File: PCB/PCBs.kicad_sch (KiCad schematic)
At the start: 55 parts, among them CN1 W2A41C681KAT2A, CN2 W2A41C681KAT2A, CN3 W2A41C681KAT2A, CN4 W2A41C681KAT2A, CN6 W2A41C681KAT2A, U1 ADS1299IPAGR, U10 TPD4E1B06DCKR, U11 TPS61023DRLR, U3 TPD4E1B06DCKR, U4 TPD4E1B06DCKR, U5 TPS73225DBVR, U6 TPD4E1B06DCKR, U7 LM2664M6, U8 TPS73233DBVT, U9 TPS72325DBVT

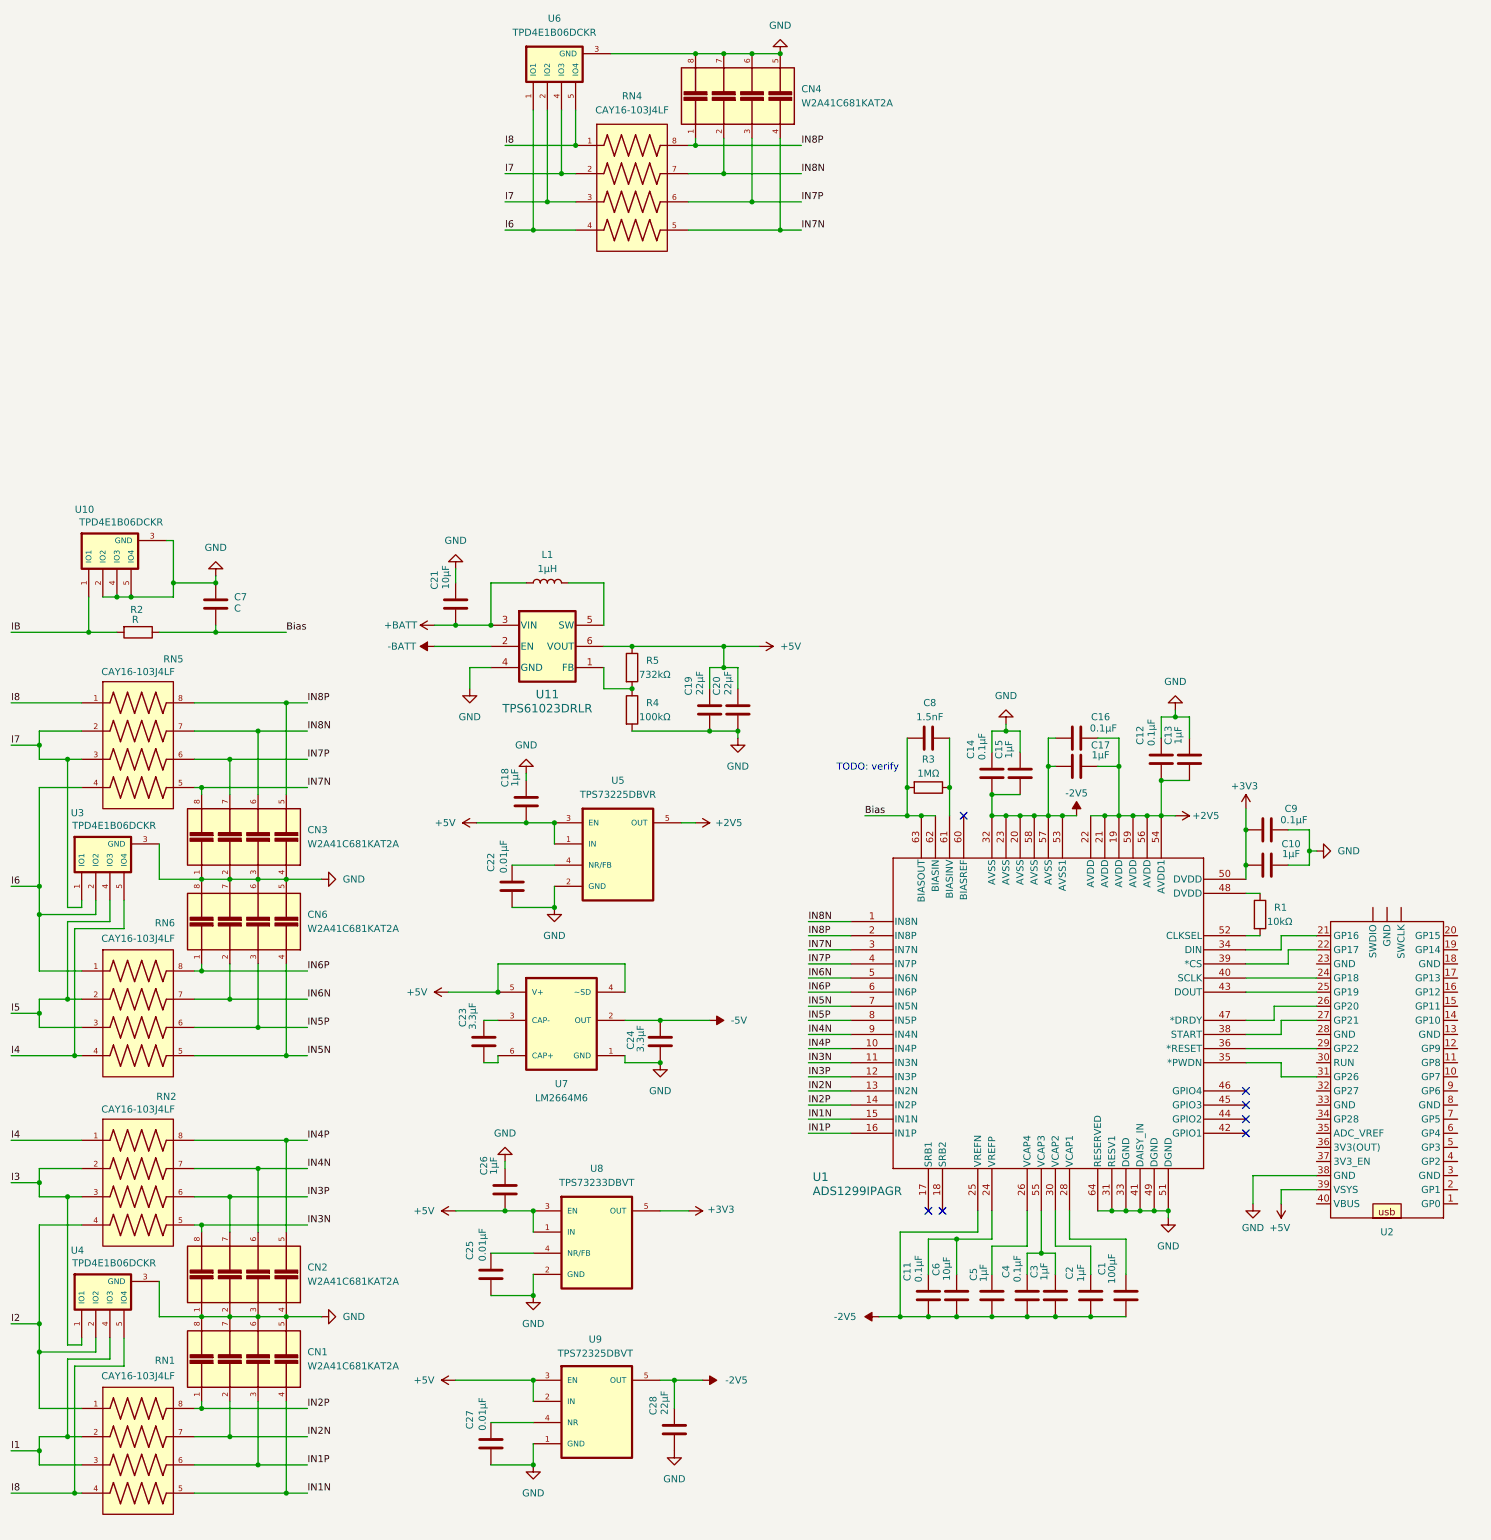
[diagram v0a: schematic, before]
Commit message: v0.1 schematic finishing touches
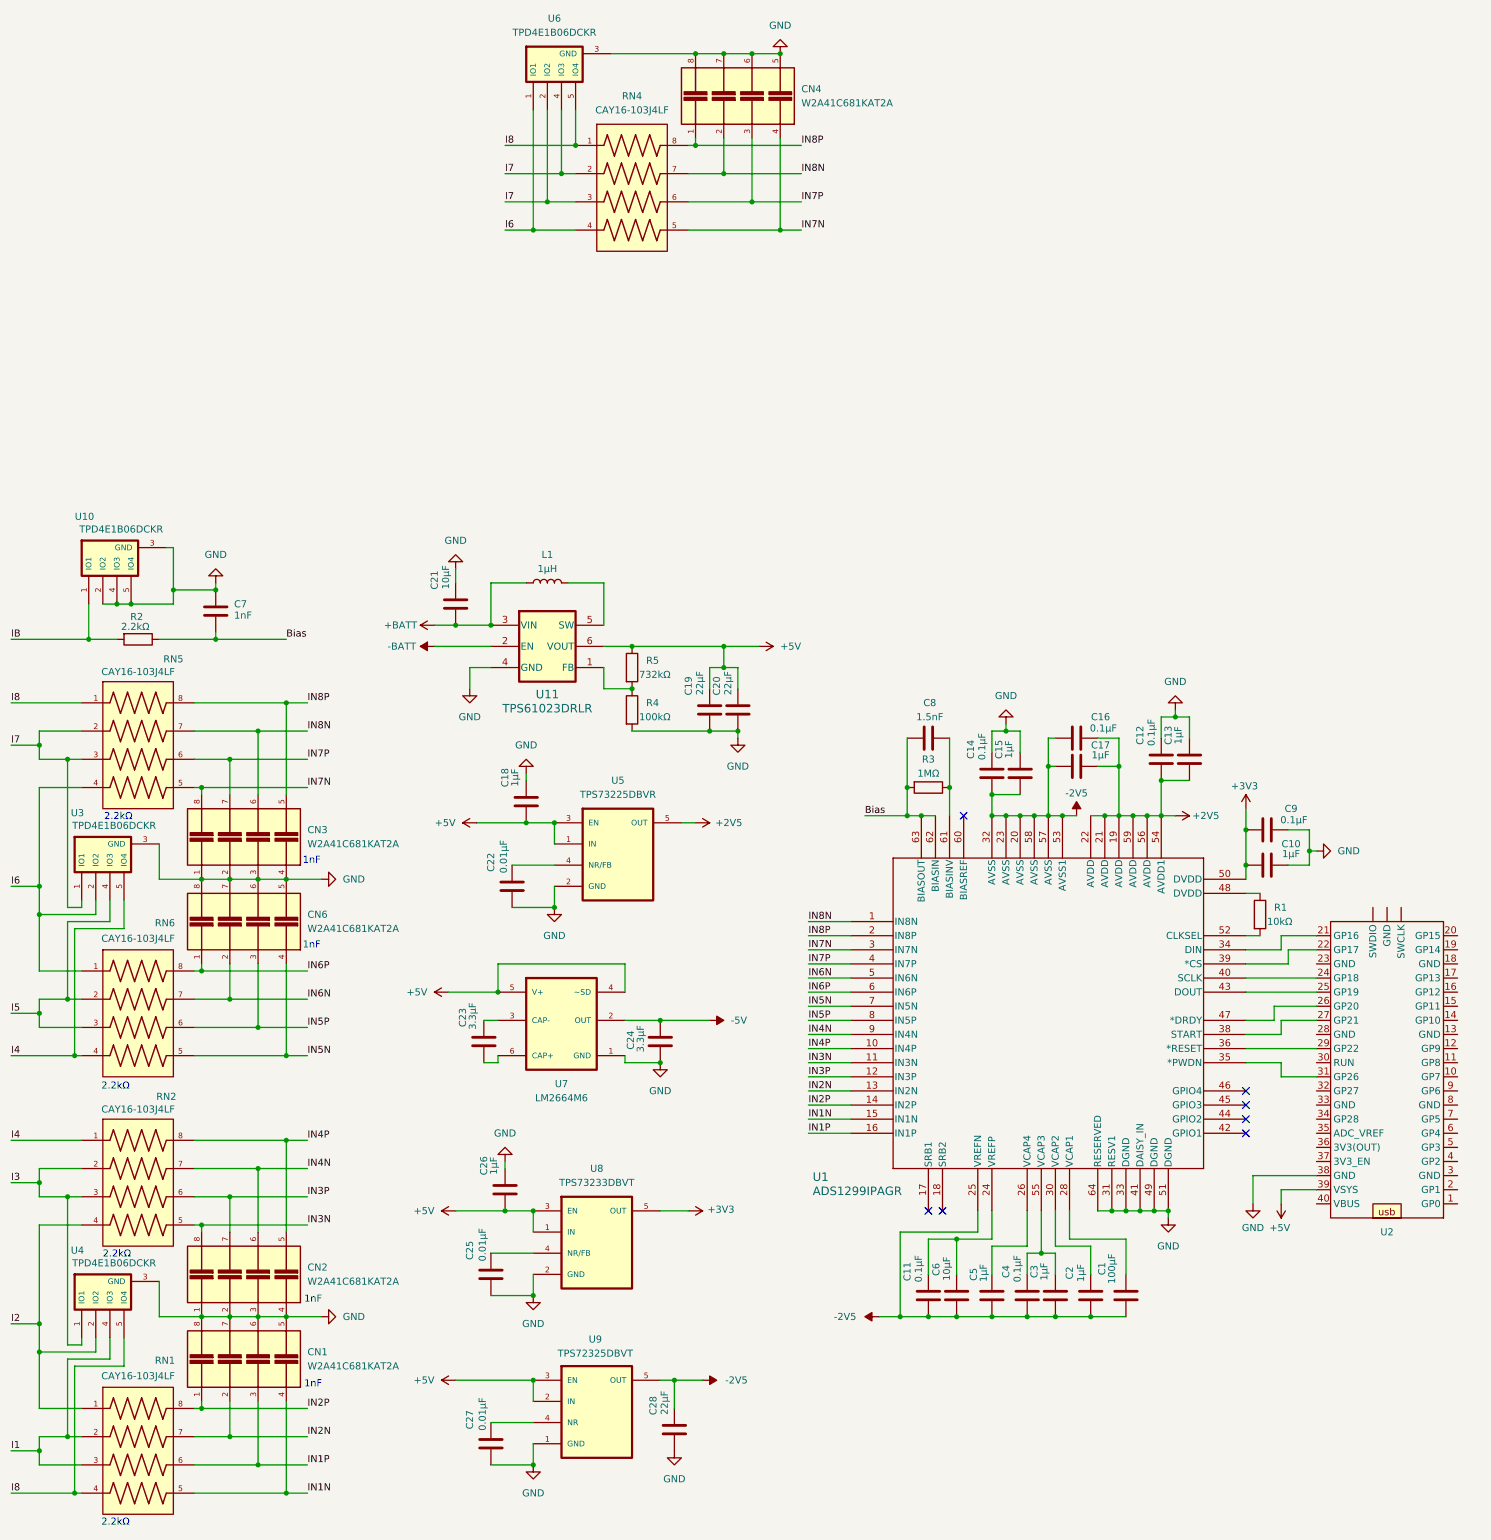
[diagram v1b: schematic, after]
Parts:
- C7: value C -> 1nF
- R2: value R -> 2.2kΩ
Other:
- note added: "1nF"
- note added: "2.2kΩ"
- note removed: "TODO: verify"
- moved on the sheet: C7, R2, U10
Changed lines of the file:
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@@
 	)
 	(junction
-		(at 39.37 27.94)
+		(at 39.37 29.21)
 		(diameter 0)
 		(color 0 0 0 0)
@@
 	)
 	(junction
-		(at 36.83 27.94)
+		(at 36.83 29.21)
 		(diameter 0)
 		(color 0 0 0 0)
@@
 	)
 	(junction
-		(at 31.75 34.29)
+		(at 31.75 35.56)
 		(diameter 0)
 		(color 0 0 0 0)
@@
 	)
 	(junction
-		(at 54.61 34.29)
+		(at 54.61 35.56)
 		(diameter 0)
 		(color 0 0 0 0)
@@
 	)
 	(junction
-		(at 46.99 25.4)
+		(at 46.99 26.67)
 		(diameter 0)
 		(color 0 0 0 0)
 	)
 	(junction
-		(at 54.61 25.4)
+		(at 54.61 26.67)
 		(diameter 0)
 		(color 0 0 0 0)
@@
 	(wire
 		(pts
-			(xy 54.61 24.13) (xy 54.61 25.4)
+			(xy 54.61 25.4) (xy 54.61 26.67)
 		)
 		(stroke
@@
 	(wire
 		(pts
-			(xy 36.83 27.94) (xy 39.37 27.94)
+			(xy 36.83 29.21) (xy 39.37 29.21)
 		)
 		(stroke
@@
 	(wire
 		(pts
-			(xy 31.75 27.94) (xy 31.75 34.29)
+			(xy 31.75 29.21) (xy 31.75 35.56)
 		)
 		(stroke
@@
 	(wire
 		(pts
-			(xy 46.99 27.94) (xy 46.99 25.4)
+			(xy 46.99 29.21) (xy 46.99 26.67)
 		)
 		(stroke
@@
 	(wire
 		(pts
-			(xy 17.78 34.29) (xy 31.75 34.29)
+			(xy 17.78 35.56) (xy 31.75 35.56)
 		)
 		(stroke
@@
 	(wire
 		(pts
-			(xy 54.61 34.29) (xy 54.61 33.02)
+			(xy 54.61 35.56) (xy 54.61 34.29)
 		)
 		(stroke
@@
 	(wire
 		(pts
-			(xy 46.99 17.78) (xy 46.99 25.4)
+			(xy 46.99 19.05) (xy 46.99 26.67)
 		)
 		(stroke
@@
 	(wire
 		(pts
-			(xy 39.37 27.94) (xy 46.99 27.94)
+			(xy 39.37 29.21) (xy 46.99 29.21)
 		)
 		(stroke
@@
 	(wire
 		(pts
-			(xy 31.75 34.29) (xy 36.83 34.29)
+			(xy 31.75 35.56) (xy 36.83 35.56)
 		)
 		(stroke
@@
 	(wire
 		(pts
-			(xy 44.45 34.29) (xy 54.61 34.29)
+			(xy 44.45 35.56) (xy 54.61 35.56)
 		)
 		(stroke
@@
 	(wire
 		(pts
-			(xy 34.29 27.94) (xy 36.83 27.94)
+			(xy 34.29 29.21) (xy 36.83 29.21)
 		)
 		(stroke
@@
 	(wire
 		(pts
-			(xy 67.31 34.29) (xy 54.61 34.29)
+			(xy 67.31 35.56) (xy 54.61 35.56)
 		)
 		(stroke
@@
 	(wire
 		(pts
-			(xy 46.99 25.4) (xy 54.61 25.4)
+			(xy 46.99 26.67) (xy 54.61 26.67)
 		)
 		(stroke
@@
 	(wire
 		(pts
-			(xy 45.72 17.78) (xy 46.99 17.78)
+			(xy 45.72 19.05) (xy 46.99 19.05)
 		)
 		(stroke
@@
 		)
 	)
-	(text "TODO: verify\n"
+	(text "2.2kΩ"
 		(exclude_from_sim no)
-		(at 171.958 58.674 0)
+		(at 36.576 116.078 0)
+		(effects
+			(font
+				(size 1.27 1.27)
+			)
+		)
+	)
+	(text "2.2kΩ"
+		(exclude_from_sim no)
+		(at 36.576 194.564 0)
+		(effects
+			(font
+				(size 1.27 1.27)
+			)
+		)
+	)
+	(text "2.2kΩ"
+		(exclude_from_sim no)
+		(at 36.83 146.304 0)
+		(effects
+			(font
+				(size 1.27 1.27)
+			)
+		)
+	)
+	(text "2.2kΩ"
+		(exclude_from_sim no)
+		(at 37.084 67.564 0)
+		(effects
+			(font
+				(size 1.27 1.27)
+			)
+		)
+	)
+	(text "1nF"
+		(exclude_from_sim no)
+		(at 71.882 90.678 0)
+		(effects
+			(font
+				(size 1.27 1.27)
+			)
+		)
+	)
+	(text "1nF"
+		(exclude_from_sim no)
+		(at 71.882 75.438 0)
+		(effects
+			(font
+				(size 1.27 1.27)
+			)
+		)
+	)
+	(text "1nF"
+		(exclude_from_sim no)
+		(at 72.136 169.672 0)
+		(effects
+			(font
+				(size 1.27 1.27)
+			)
+		)
+	)
+	(text "1nF"
+		(exclude_from_sim no)
+		(at 72.136 154.432 0)
 		(effects
 			(font
@@
 	)
 	(label "Bias"
-		(at 67.31 34.29 0)
+		(at 67.31 35.56 0)
 		(fields_autoplaced yes)
 		(effects
@@
 	)
 	(label "IB"
-		(at 17.78 34.29 0)
+		(at 17.78 35.56 0)
 		(fields_autoplaced yes)
 		(effects
@@
 	(symbol
 		(lib_id "Device:R")
-		(at 40.64 34.29 270)
+		(at 40.64 35.56 270)
 		(unit 1)
 		(exclude_from_sim no)
@@
 		(dnp no)
 		(property "Reference" "R2"
-			(at 40.386 30.226 90)
+			(at 40.386 31.496 90)
 			(effects
 				(font
@@
 			)
 		)
-		(property "Value" "R"
-			(at 40.132 32.004 90)
+		(property "Value" "2.2kΩ"
+			(at 40.132 33.274 90)
 			(effects
 				(font
@@
 		)
 		(property "Footprint" ""
-			(at 40.64 32.512 90)
+			(at 40.64 33.782 90)
 			(effects
 				(font
@@
 		)
 		(property "Datasheet" "~"
-			(at 40.64 34.29 0)
+			(at 40.64 35.56 0)
 			(effects
 				(font
@@
 		)
 		(property "Description" "Resistor"
-			(at 40.64 34.29 0)
+			(at 40.64 35.56 0)
 			(effects
 				(font
@@
 	(symbol
 		(lib_id "Device:C")
-		(at 54.61 29.21 0)
+		(at 54.61 30.48 0)
 		(unit 1)
 		(exclude_from_sim no)
@@
 		(dnp no)
 		(property "Reference" "C7"
-			(at 57.912 27.94 0)
+			(at 57.912 29.21 0)
 			(effects
 				(font
@@
 			)
 		)
-		(property "Value" "C"
-			(at 57.912 29.972 0)
+		(property "Value" "1nF"
+			(at 57.912 31.242 0)
 			(effects
 				(font
@@
 		)
 		(property "Footprint" ""
-			(at 55.5752 33.02 0)
+			(at 55.5752 34.29 0)
 			(effects
 				(font
@@
 		)
 		(property "Datasheet" "~"
-			(at 54.61 29.21 0)
+			(at 54.61 30.48 0)
 			(effects
 				(font
@@
 		)
 		(property "Description" "Unpolarized capacitor"
-			(at 54.61 29.21 0)
+			(at 54.61 30.48 0)
 			(effects
 				(font
@@
 		(lib_name "TPD4E1B06DCKR_1")
 		(lib_id "custom_lib:TPD4E1B06DCKR")
-		(at 43.18 24.13 0)
+		(at 43.18 25.4 0)
 		(unit 1)
 		(exclude_from_sim no)
@@
 		(dnp no)
 		(property "Reference" "U10"
-			(at 30.988 12.192 0)
+			(at 30.988 13.462 0)
 			(effects
 				(font
@@
 		)
 		(property "Value" "TPD4E1B06DCKR"
-			(at 37.592 14.478 0)
+			(at 37.592 15.748 0)
 			(effects
 				(font
@@
 		)
 		(property "Footprint" "TPD4E1B06DCKR:SOT65P210X110-6N"
-			(at 41.402 49.784 0)
+			(at 41.402 51.054 0)
 			(effects
 				(font
@@
 		)
 		(property "Datasheet" ""
-			(at 43.18 24.13 0)
+			(at 43.18 25.4 0)
 			(effects
 				(font
@@
 		)
 		(property "Description" ""
-			(at 43.18 24.13 0)
+			(at 43.18 25.4 0)
 			(effects
 				(font
@@
 		)
 		(property "MF" "Texas Instruments"
-			(at 62.738 39.624 0)
+			(at 62.738 40.894 0)
 			(effects
 				(font
@@
 		)
 		(property "Description_1" "\nQuad 0.7-pF, ±5.5-V, ±12-kV ESD protection diode with 0.5-nA max leakage in SOT & SC70 packages\n"
-			(at 42.418 41.656 0)
+			(at 42.418 42.926 0)
 			(effects
 				(font
@@
 		)
 		(property "Package" "SOT-SC70-6 Texas Instruments"
-			(at 10.668 38.608 0)
+			(at 10.668 39.878 0)
 			(effects
 				(font
@@
 		)
 		(property "Price" "None"
-			(at 50.038 -7.62 0)
+			(at 50.038 -6.35 0)
 			(effects
 				(font
@@
 		)
 		(property "SnapEDA_Link" "https://www.snapeda.com/parts/TPD4E1B06DCKR/Texas+Instruments/view-part/?ref=snap"
-			(at 40.894 44.45 0)
+			(at 40.894 45.72 0)
 			(effects
 				(font
@@
 		)
 		(property "MP" "TPD4E1B06DCKR"
-			(at 28.956 -5.334 0)
+			(at 28.956 -4.064 0)
 			(effects
 				(font
@@
 		)
 		(property "Purchase-URL" "https://www.snapeda.com/api/url_track_click_mouser/?unipart_id=46121&manufacturer=Texas Instruments&part_name=TPD4E1B06DCKR&search_term=None"
-			(at 43.942 52.832 0)
+			(at 43.942 54.102 0)
 			(effects
 				(font
@@
 		)
 		(property "Availability" "In Stock"
-			(at 53.086 -1.524 0)
+			(at 53.086 -0.254 0)
 			(effects
 				(font
@@
 		)
 		(property "Check_prices" "https://www.snapeda.com/parts/TPD4E1B06DCKR/Texas+Instruments/view-part/?ref=eda"
-			(at 42.926 46.736 0)
+			(at 42.926 48.006 0)
 			(effects
 				(font
@@
 	(symbol
 		(lib_id "power:GND")
-		(at 54.61 24.13 180)
+		(at 54.61 25.4 180)
 		(unit 1)
 		(exclude_from_sim no)
@@
 		(fields_autoplaced yes)
 		(property "Reference" "#PWR05"
-			(at 54.61 17.78 0)
+			(at 54.61 19.05 0)
 			(effects
 				(font
@@
 		)
 		(property "Value" "GND"
-			(at 54.61 19.05 0)
+			(at 54.61 20.32 0)
 			(effects
 				(font
@@
 		)
 		(property "Footprint" ""
-			(at 54.61 24.13 0)
+			(at 54.61 25.4 0)
 			(effects
 				(font
@@
 		)
 		(property "Datasheet" ""
-			(at 54.61 24.13 0)
+			(at 54.61 25.4 0)
 			(effects
 				(font
@@
 		)
 		(property "Description" "Power symbol creates a global label with name \"GND\" , ground"
-			(at 54.61 24.13 0)
+			(at 54.61 25.4 0)
 			(effects
 				(font

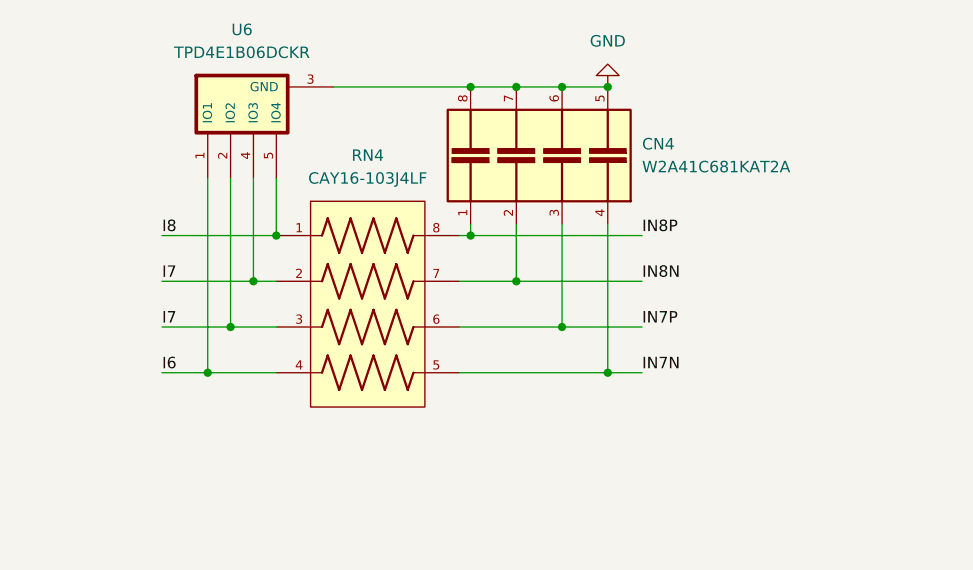
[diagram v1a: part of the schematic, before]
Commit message: removed old input schem
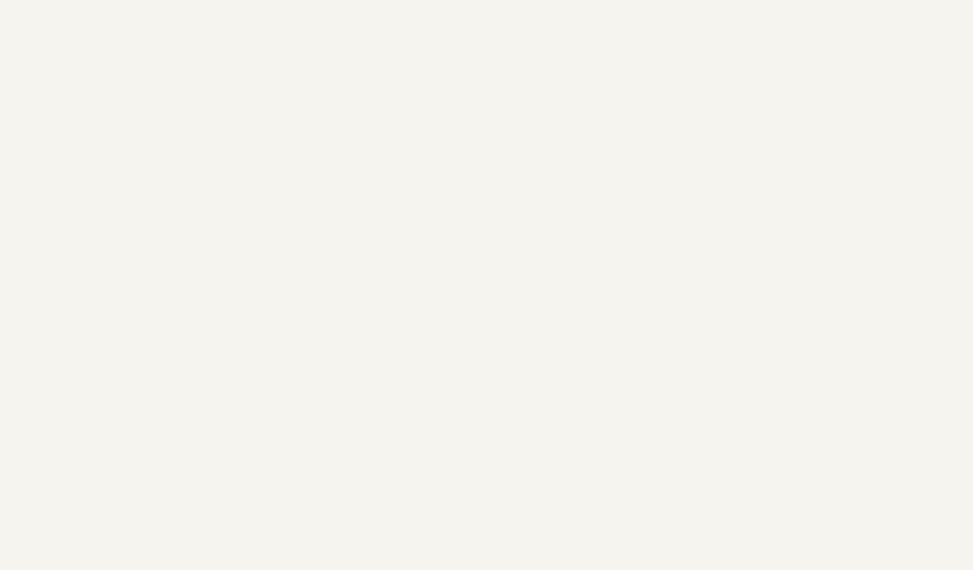
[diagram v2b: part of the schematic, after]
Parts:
- removed CN4: W2A41C681KAT2A, W2A41C681KAT2A:CAPCAXE50P210X130X94-8N, symbol custom_lib:W2A41C681KAT2A
- removed RN4: CAY16-103J4LF, CAY16-103J4LF:RESCAF80P320X160X60-8N, symbol custom_lib:CAY16-103J4LF
- removed U6: TPD4E1B06DCKR, TPD4E1B06DCKR:SOT65P210X110-6N, symbol custom_lib:TPD4E1B06DCKR
